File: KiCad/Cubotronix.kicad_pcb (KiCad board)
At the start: 2 copper layers, 35 x 35 mm, 32 parts, among them J1 Vin, J2 ADC, J3 GPIO12, J4 GPIO15, P2 Battery, P5 USB-Serial, P6 I2C/1-W, SW1 Boot, SW2 Reset, U1 AP2114H-3.3TRG1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

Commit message: Vias fixes
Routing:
- net +3V3: track 104.1 -> 111.2 mm
- net /ADC: track 40.3 -> 46.1 mm
- net GND: track 88.6 -> 84.7 mm
- net VCC: track 67.1 -> 69.0 mm
- net /TX: track 24.2 -> 24.8 mm
- net Net-(C1-Pad1): track 27.7 -> 27.1 mm

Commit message: change on/off pin
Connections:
- C1 pad 1: Net-(C1-Pad1) -> VCC
- JP1 pad 2: Net-(C1-Pad1) -> VCC
- U1 pad 3: Net-(C1-Pad1) -> VCC
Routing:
- net VCC: track 69.0 -> 98.7 mm
- net Net-(C1-Pad1): track 27.1 -> 0.00 mm
- net (no net): track 0.00 -> 4.60 mm, vias 0 -> 4
- net GND: track 84.7 -> 80.1 mm, vias 16 -> 12
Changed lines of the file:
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@@
 (kicad_pcb (version 4) (host pcbnew 4.0.7)
   (general
-    (links 65)
-    (no_connects 0)
+    (links 66)
+    (no_connects 2)
     (area 114.949999 54.949999 150.050001 90.050001)
     (thickness 1.6)
     (drawings 24)
-    (tracks 362)
+    (tracks 363)
     (zones 0)
     (modules 32)
-    (nets 28)
+    (nets 27)
   )
   (page A4)
@@
   (net 25 /GPIO14)
   (net 26 /GPIO13)
-  (net 27 "Net-(C1-Pad1)")
   (net_class Default "Esta es la clase de red por defecto."
     (clearance 0.2)
@@
     (add_net /TX)
     (add_net GND)
-    (add_net "Net-(C1-Pad1)")
     (add_net VCC)
   )
@@
     (fp_line (start -0.5 -0.85) (end 0.5 -0.85) (layer B.SilkS) (width 0.15))
     (pad 1 smd rect (at -1.25 0 270) (size 1.5 1.25) (layers B.Cu B.Paste B.Mask)
-      (net 27 "Net-(C1-Pad1)"))
+      (net 1 VCC))
     (pad 2 smd rect (at 1.25 0 270) (size 1.5 1.25) (layers B.Cu B.Paste B.Mask)
       (net 2 GND))
@@
       (net 1 VCC))
     (pad 2 thru_hole oval (at 0 2.54 180) (size 1.7 1.7) (drill 1) (layers *.Cu *.Mask)
-      (net 27 "Net-(C1-Pad1)"))
+      (net 1 VCC))
     (model ${KISYS3DMOD}/Pin_Headers.3dshapes/Pin_Header_Straight_1x02_Pitch2.54mm.wrl
       (at (xyz 0 0 0))
@@
       (net 3 +3V3))
     (pad 3 smd rect (at -3.15 -2.3 90) (size 2 1.5) (layers B.Cu B.Paste B.Mask)
-      (net 27 "Net-(C1-Pad1)"))
+      (net 1 VCC))
     (pad 1 smd rect (at -3.15 2.3 90) (size 2 1.5) (layers B.Cu B.Paste B.Mask)
       (net 2 GND))
@@
     (arrow2b (pts (xy 115 95) (xy 116.126504 94.413579)))
   )
+  (segment (start 137.75 72.75) (end 136.5 72.75) (width 0.5) (layer F.Cu) (net 0))
+  (via (at 136.5 72.75) (size 0.8) (drill 0.6) (layers F.Cu B.Cu) (net 0))
+  (segment (start 139 72.75) (end 137.75 72.75) (width 0.5) (layer B.Cu) (net 0))
+  (via (at 137.75 72.75) (size 0.8) (drill 0.6) (layers F.Cu B.Cu) (net 0))
+  (segment (start 140.15 72.75) (end 139 72.75) (width 0.5) (layer F.Cu) (net 0))
+  (via (at 139 72.75) (size 0.8) (drill 0.6) (layers F.Cu B.Cu) (net 0))
+  (segment (start 140.75 73.45) (end 140.15 72.85) (width 0.5) (layer B.Cu) (net 0))
+  (segment (start 140.15 72.85) (end 140.15 72.75) (width 0.5) (layer B.Cu) (net 0))
+  (via (at 140.15 72.75) (size 0.8) (drill 0.6) (layers F.Cu B.Cu) (net 0))
+  (segment (start 147.9 84.06) (end 147.9 86.6) (width 0.5) (layer B.Cu) (net 1))
   (segment (start 142.95 86.2) (end 143.2 86.45) (width 0.5) (layer F.Cu) (net 1))
   (segment (start 142.95 86.2) (end 133.15 86.2) (width 0.5) (layer F.Cu) (net 1))
@@
   (segment (start 147.9 86.6) (end 146.55 86.6) (width 0.5) (layer B.Cu) (net 1))
   (segment (start 143.9 77.13) (end 142.945 77.13) (width 0.5) (layer B.Cu) (net 1))
+  (segment (start 147.9 84.06) (end 146.697919 84.06) (width 0.5) (layer B.Cu) (net 1))
+  (segment (start 146.2 83.562081) (end 146.2 76.9) (width 0.5) (layer B.Cu) (net 1))
+  (segment (start 146.2 76.9) (end 145.75 76.45) (width 0.5) (layer B.Cu) (net 1))
+  (segment (start 146.697919 84.06) (end 146.2 83.562081) (width 0.5) (layer B.Cu) (net 1))
+  (segment (start 145.75 76.45) (end 145.75 70.8) (width 0.5) (layer B.Cu) (net 1))
+  (segment (start 145.75 70.8) (end 145.25 70.3) (width 0.5) (layer B.Cu) (net 1))
+  (segment (start 145.25 70.3) (end 143.6 70.3) (width 0.5) (layer B.Cu) (net 1))
+  (segment (start 142.9 69.6) (end 142.9 66.9) (width 0.5) (layer B.Cu) (net 1))
+  (segment (start 143.6 70.3) (end 142.9 69.6) (width 0.5) (layer B.Cu) (net 1))
+  (segment (start 142.9 66.9) (end 142.9 63.45) (width 0.5) (layer B.Cu) (net 1))
+  (segment (start 142.9 63.45) (end 140.25 63.45) (width 0.5) (layer B.Cu) (net 1))
+  (segment (start 140.25 63.45) (end 140.2 63.4) (width 0.5) (layer B.Cu) (net 1))
+  (segment (start 142.95 63.5) (end 142.9 63.45) (width 0.3) (layer B.Cu) (net 1))
   (segment (start 148.1 78.92) (end 148.1 80.122081) (width 0.5) (layer B.Cu) (net 2))
   (segment (start 148.1 80.122081) (end 149.4 81.422081) (width 0.5) (layer B.Cu) (net 2))
@@
   (segment (start 140.2 70.25) (end 141.75 70.25) (width 0.5) (layer B.Cu) (net 2))
   (via (at 141.75 70.25) (size 0.8) (drill 0.6) (layers F.Cu B.Cu) (net 2))
-  (segment (start 137.75 72.75) (end 136.5 72.75) (width 0.5) (layer F.Cu) (net 2))
-  (via (at 136.5 72.75) (size 0.8) (drill 0.6) (layers F.Cu B.Cu) (net 2))
-  (segment (start 139 72.75) (end 137.75 72.75) (width 0.5) (layer B.Cu) (net 2))
-  (via (at 137.75 72.75) (size 0.8) (drill 0.6) (layers F.Cu B.Cu) (net 2))
-  (segment (start 140.15 72.75) (end 139 72.75) (width 0.5) (layer F.Cu) (net 2))
-  (via (at 139 72.75) (size 0.8) (drill 0.6) (layers F.Cu B.Cu) (net 2))
   (segment (start 142.7 89.35) (end 141.15 89.35) (width 0.5) (layer F.Cu) (net 2))
   (segment (start 140.66 88) (end 140.66 88.86) (width 0.5) (layer F.Cu) (net 2))
@@
   (segment (start 140.2 65.9) (end 140.2 70.25) (width 0.5) (layer B.Cu) (net 2))
   (via (at 140.2 70.25) (size 0.8) (drill 0.6) (layers F.Cu B.Cu) (net 2))
-  (segment (start 140.75 73.45) (end 140.15 72.85) (width 0.5) (layer B.Cu) (net 2))
-  (segment (start 140.15 72.85) (end 140.15 72.75) (width 0.5) (layer B.Cu) (net 2))
-  (via (at 140.15 72.75) (size 0.8) (drill 0.6) (layers F.Cu B.Cu) (net 2))
   (segment (start 142.575 79.4) (end 142.45 79.4) (width 0.5) (layer B.Cu) (net 2))
   (via (at 118.2 85) (size 0.8) (drill 0.6) (layers F.Cu B.Cu) (net 3))
@@
   (segment (start 138.7 65.25) (end 139 64.95) (width 0.3) (layer F.Cu) (net 23))
   (segment (start 139 64.95) (end 139 59.7) (width 0.3) (layer F.Cu) (net 23))
-  (segment (start 147.9 84.06) (end 146.697919 84.06) (width 0.5) (layer B.Cu) (net 27))
-  (segment (start 146.2 83.562081) (end 146.2 76.9) (width 0.5) (layer B.Cu) (net 27))
-  (segment (start 146.2 76.9) (end 145.75 76.45) (width 0.5) (layer B.Cu) (net 27))
-  (segment (start 146.697919 84.06) (end 146.2 83.562081) (width 0.5) (layer B.Cu) (net 27))
-  (segment (start 145.75 76.45) (end 145.75 70.8) (width 0.5) (layer B.Cu) (net 27))
-  (segment (start 145.75 70.8) (end 145.25 70.3) (width 0.5) (layer B.Cu) (net 27))
-  (segment (start 145.25 70.3) (end 143.6 70.3) (width 0.5) (layer B.Cu) (net 27))
-  (segment (start 142.9 69.6) (end 142.9 66.9) (width 0.5) (layer B.Cu) (net 27))
-  (segment (start 143.6 70.3) (end 142.9 69.6) (width 0.5) (layer B.Cu) (net 27))
-  (segment (start 142.9 66.9) (end 142.9 63.45) (width 0.5) (layer B.Cu) (net 27))
-  (segment (start 142.9 63.45) (end 140.25 63.45) (width 0.5) (layer B.Cu) (net 27))
-  (segment (start 140.25 63.45) (end 140.2 63.4) (width 0.5) (layer B.Cu) (net 27))
-  (segment (start 142.95 63.5) (end 142.9 63.45) (width 0.3) (layer B.Cu) (net 27))
   (zone (net 0) (net_name "") (layer F.Cu) (hatch edge 0.508)
     (connect_pads (clearance 0.508))

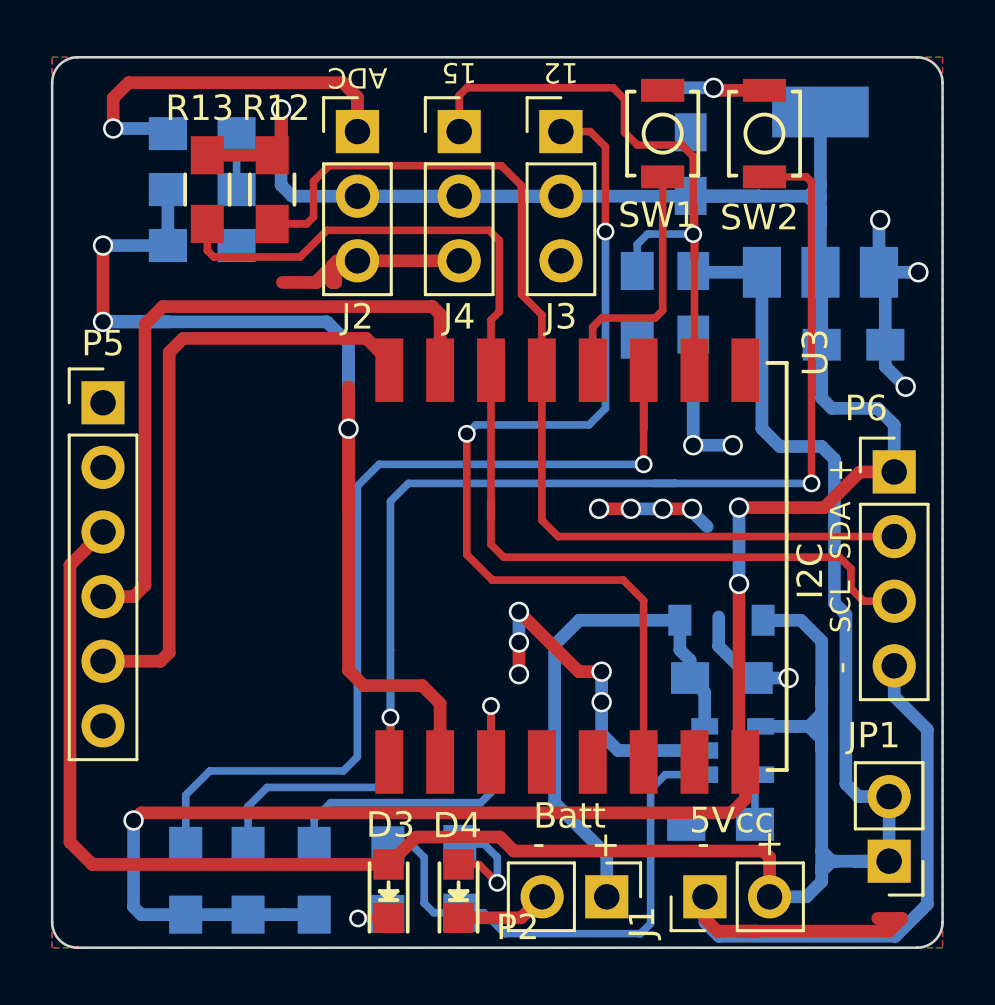
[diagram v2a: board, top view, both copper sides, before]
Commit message: Add labels
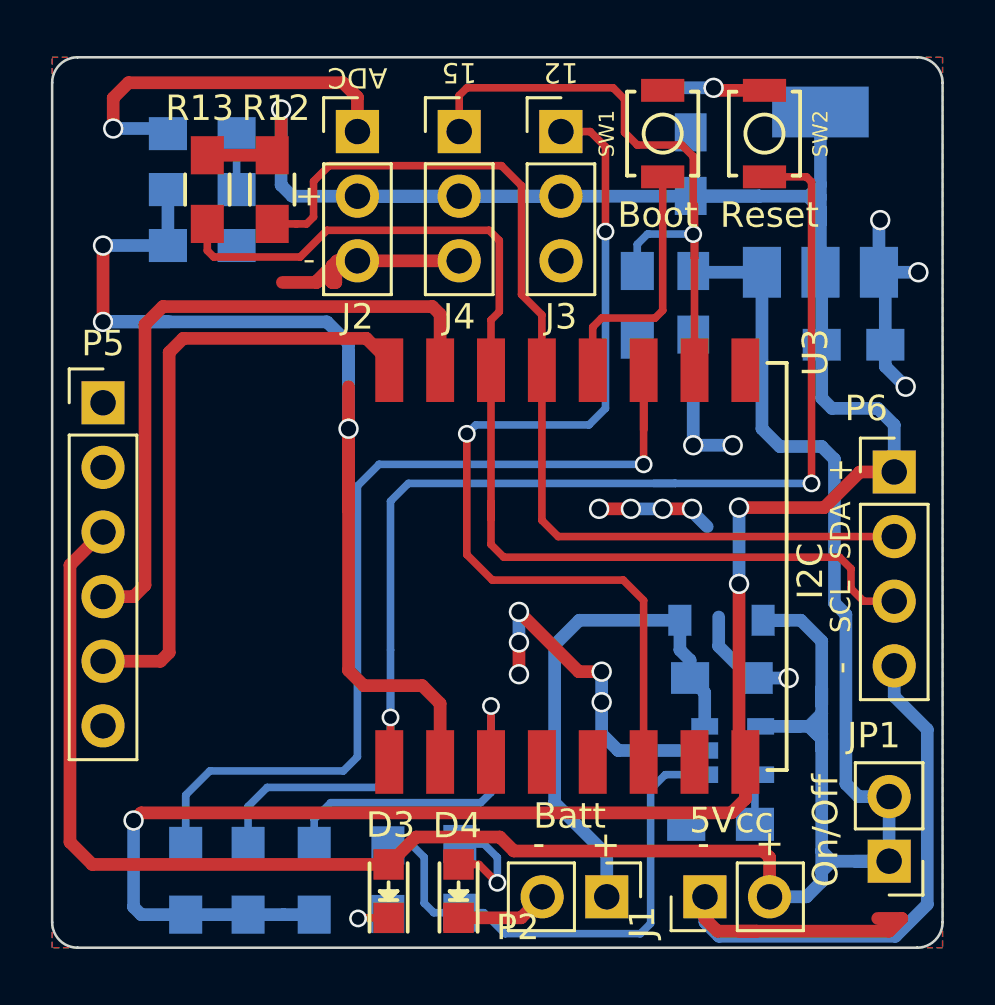
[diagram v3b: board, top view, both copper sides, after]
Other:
- board text added: "0.1v 04/2018"
- board text added: "Cubotronix"
- board text added: "Designed by: @foreverwero"
- board text added: "On/Off"
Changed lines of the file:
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@@
     (area 114.949999 54.949999 150.050001 90.050001)
     (thickness 1.6)
-    (drawings 24)
+    (drawings 30)
     (tracks 363)
     (zones 0)
@@
   )
   (layers
-    (0 F.Cu signal)
-    (31 B.Cu signal)
+    (0 F.Cu signal hide)
+    (31 B.Cu signal hide)
     (32 B.Adhes user)
     (33 F.Adhes user)
@@
     (47 F.CrtYd user)
     (48 B.Fab user hide)
-    (49 F.Fab user hide)
+    (49 F.Fab user)
   )
   (setup
@@
     (tags "Tactile Switch")
     (attr smd)
-    (fp_text reference SW1 (at 3.2 0.2 360) (layer F.SilkS)
-      (effects (font (size 1 1) (thickness 0.15)))
-    )
-    (fp_text value Boot (at 0 2.5 270) (layer F.Fab)
+    (fp_text reference SW1 (at 0 2.2 270) (layer F.SilkS)
+      (effects (font (size 0.6 0.6) (thickness 0.1)))
+    )
+    (fp_text value Boot (at 3.2 0.2 360) (layer F.SilkS)
       (effects (font (size 1 1) (thickness 0.15)))
     )
@@
     (tags "Tactile Switch")
     (attr smd)
-    (fp_text reference SW2 (at 3.3 0.2 360) (layer F.SilkS)
-      (effects (font (size 1 1) (thickness 0.15)))
-    )
-    (fp_text value Reset (at 0 2.5 270) (layer F.Fab)
+    (fp_text reference SW2 (at 0 -2.2 450) (layer F.SilkS)
+      (effects (font (size 0.6 0.6) (thickness 0.1)))
+    )
+    (fp_text value Reset (at 3.2 -0.2 360) (layer F.SilkS)
       (effects (font (size 1 1) (thickness 0.15)))
     )
@@
     )
   )
+  (gr_text - (at 125.1 62.95) (layer F.SilkS)
+    (effects (font (size 0.8 1) (thickness 0.2)))
+  )
+  (gr_text + (at 125.1 60.45) (layer F.SilkS)
+    (effects (font (size 0.8 1) (thickness 0.2)))
+  )
+  (gr_text "Cubotronix " (at 122 75 90) (layer B.SilkS)
+    (effects (font (size 1.5 1.5) (thickness 0.3)) (justify mirror))
+  )
+  (gr_text "Designed by: \n@foreverwero" (at 133.6 75.6 90) (layer B.SilkS)
+    (effects (font (size 1.5 1.5) (thickness 0.3)) (justify mirror))
+  )
+  (gr_text "0.1v\n04/2018" (at 127 74.6 90) (layer B.SilkS)
+    (effects (font (size 1.5 1.5) (thickness 0.3)) (justify mirror))
+  )
+  (gr_text "On/Off\n" (at 145.4 85.4 90) (layer F.SilkS)
+    (effects (font (size 1 1) (thickness 0.2)))
+  )
   (gr_text 12 (at 135 55.6 180) (layer F.SilkS)

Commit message: add gerber
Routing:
- net /ADC: track 46.1 -> 41.2 mm
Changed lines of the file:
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@@
   (general
     (links 66)
-    (no_connects 2)
-    (area 114.949999 54.949999 150.050001 90.050001)
+    (no_connects 1)
+    (area 82.150001 53.07619 150.125001 97.700001)
     (thickness 1.6)
     (drawings 30)
-    (tracks 363)
+    (tracks 362)
     (zones 0)
     (modules 32)
@@
   )
   (layers
-    (0 F.Cu signal hide)
-    (31 B.Cu signal hide)
-    (32 B.Adhes user)
-    (33 F.Adhes user)
-    (34 B.Paste user)
-    (35 F.Paste user)
+    (0 F.Cu signal)
+    (31 B.Cu signal)
+    (32 B.Adhes user hide)
+    (33 F.Adhes user hide)
+    (34 B.Paste user hide)
+    (35 F.Paste user hide)
     (36 B.SilkS user)
     (37 F.SilkS user)
     (38 B.Mask user)
     (39 F.Mask user)
-    (40 Dwgs.User user)
-    (41 Cmts.User user)
-    (42 Eco1.User user)
-    (43 Eco2.User user)
+    (40 Dwgs.User user hide)
+    (41 Cmts.User user hide)
+    (42 Eco1.User user hide)
+    (43 Eco2.User user hide)
     (44 Edge.Cuts user)
     (45 Margin user)
@@
     (47 F.CrtYd user)
     (48 B.Fab user hide)
-    (49 F.Fab user)
+    (49 F.Fab user hide)
   )
   (setup
@@
     (visible_elements FFFFFF7F)
     (pcbplotparams
-      (layerselection 0x010f0_80000001)
+      (layerselection 0x0d0f0_80000001)
       (usegerberextensions false)
       (excludeedgelayer true)
@@
       (drillshape 0)
       (scaleselection 1)
-      (outputdirectory "../Tarjetas Produccion/Gerbers_170109/LoRaKitty/"))
+      (outputdirectory "/Volumes/Macintosh_HD/Documents/Eduardo_ Contreras_Flores/Cubotronix/Gerbers/"))
   )
   (net 0 "")
@@
   (segment (start 125.3 84.95) (end 125.95 84.3) (width 0.3) (layer B.Cu) (net 17))
   (segment (start 126.65 67.95) (end 126.65 67) (width 0.5) (layer B.Cu) (net 18))
-  (segment (start 126.65 72.8) (end 126.65 67.95) (width 0.5) (layer F.Cu) (net 18))
   (via (at 126.65 69.6) (size 0.8) (drill 0.6) (layers F.Cu B.Cu) (net 18))
   (segment (start 126.65 69.6) (end 126.65 67) (width 0.5) (layer B.Cu) (net 18))
